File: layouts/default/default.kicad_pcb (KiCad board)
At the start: 2 copper layers, 76.8 x 46.3 mm, 60 parts, among them U10 10µF ±10% 25V X5R, U11 10µF ±10% 25V X5R, U12 10µF ±10% 25V X5R, U13 1MΩ ±1% 62.5mW, U14 100nF ±10% 16V X7R, U16 1µF ±10% 25V X5R, U17 560Ω ±1% 62.5mW, U18 1µF ±10% 25V X5R, U19 4.7kΩ ±1% 62.5mW, U20 10µF ±10% 25V X5R, U21 10µF ±10% 25V X5R, U23 10kΩ ±1% 62.5mW, U25 100nF ±10% 16V X7R, U29 4.7kΩ ±1% 62.5mW, U5 820Ω ±1% 62.5mW, U6 4.7kΩ ±1% 62.5mW, U8 1.5µH ±20%, U9 10µF ±10% 25V X5R

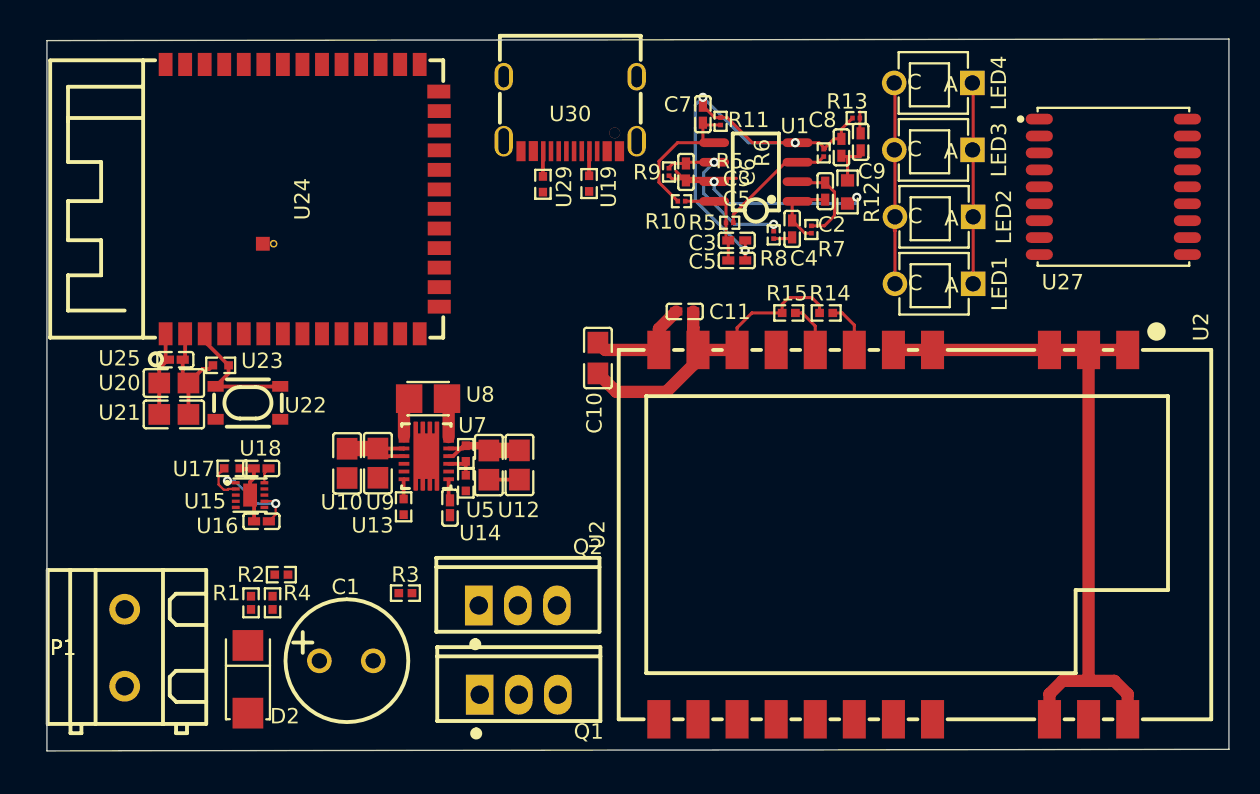
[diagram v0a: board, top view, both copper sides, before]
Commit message: added new oled
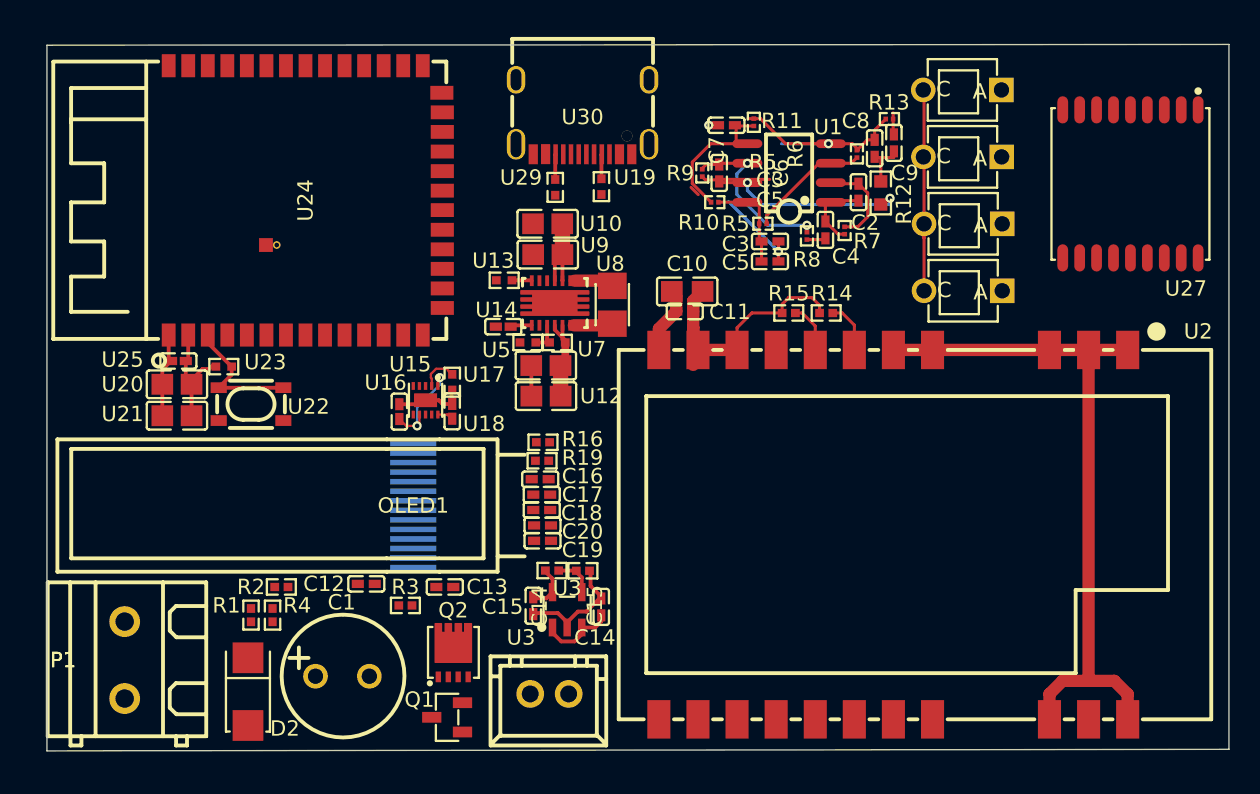
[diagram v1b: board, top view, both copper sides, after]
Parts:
- added C12: 1µF ±10% 25V X5R, atopile:C0402-b3ef17, F.Cu at (54.5, 68.8)
- added C13: 1µF ±10% 25V X5R, atopile:C0402-b3ef17, F.Cu at (59.6, 69.0)
- added C14: 1µF ±10% 25V X5R, atopile:C0402-b3ef17, F.Cu at (69.8, 70.3)
- added C15: 1µF ±10% 25V X5R, atopile:C0402-b3ef17, F.Cu at (65.4, 70.2)
- added C16: 100nF ±10% 16V X7R, atopile:C0402-b3ef17, F.Cu at (65.8, 62.0)
- added C17: 4.7µF ±20% 10V X5R, atopile:C0402-b3ef17, F.Cu at (66.0, 63.0)
- added C18: 100nF ±10% 16V X7R, atopile:C0402-b3ef17, F.Cu at (66.0, 64.0)
- added C19: 100nF ±10% 16V X7R, atopile:C0402-b3ef17, F.Cu at (66.0, 66.0)
- added C20: 100nF ±10% 16V X7R, atopile:C0402-b3ef17, F.Cu at (66.0, 65.0)
- added CN1: , atopile:CONN-TH_XH-2A-b4a6f6, F.Cu at (66.5, 76.0)
- added OLED1: , atopile:OLED-SMD_N087-2832TSWYG02-H14_1-7d3a70, F.Cu at (57.6, 63.7)
- added R16: 510kΩ ±1% 62.5mW, atopile:R0402-56259e, F.Cu at (66.0, 59.6)
- added R17: 10kΩ ±1% 62.5mW, atopile:R0402-56259e, F.Cu at (68.6, 67.9)
- added R18: 25.5kΩ ±1% 62.5mW, atopile:R0402-56259e, F.Cu at (66.6, 67.9)
- added R19: 10kΩ ±1% 62.5mW, atopile:R0402-56259e, F.Cu at (66.0, 60.8)
- added U3: , lib:SOT-23-5_L3.0-W1.7-P0.95-LS2.8-BL, F.Cu at (67.6, 70.5)
- Q1: footprint atopile:TO-220-3_L10.0-W4.5-P2.54-L-8dee21 -> atopile:SOT-23-3_L2.9-W1.3-P1.90-LS2.4-BR-688f29
- Q2: footprint atopile:TO-220-3_L10.0-W4.5-P2.54-L-8dee21 -> atopile:DFN-8_L3.3-W3.3-P0.65-BL-2-bd6bc9
- moved U10 20.3 mm to (66.3, 45.4), turned to 180 degrees
- moved U9 17.5 mm to (66.3, 47.4), turned to 180 degrees
- moved U13 16.1 mm to (63.5, 49.1), turned to 180 degrees
- moved U17 15.4 mm to (60.1, 55.7), turned to -90 degrees
- moved U8 13.4 mm to (70.5, 50.7), turned to 90 degrees
- moved U7 13.0 mm to (66.8, 50.5), turned to 0 degrees
- moved U15 13.0 mm to (58.4, 56.9), turned to 180 degrees
- moved U18 13.0 mm to (60.1, 57.6), turned to 90 degrees
- moved U14 12.3 mm to (63.4, 52.1), turned to 180 degrees
- moved U16 11.4 mm to (56.7, 57.6), turned to 90 degrees
- moved U5 9.99 mm to (65.0, 53.1), turned to 180 degrees
- moved U6 9.36 mm to (67.0, 53.1), turned to 180 degrees
- moved U11 7.45 mm to (66.2, 54.6), turned to 180 degrees
- moved C10 7.24 mm to (75.4, 49.8), turned to 180 degrees
- moved Q2 5.72 mm to (60.2, 74.1)
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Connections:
- net A5 renamed CC1
- net CC2 renamed B5
- net DN2 renamed DN1
- net DP2 renamed DP1
- net VINA renamed boostbuck-EN
- Q1 pad 2: cutoff-C-1 -> gnd
- Q1 pad 3: gnd -> cutoff-C-1
- Q2 pad 1: CUTOFF_GATE -> gnd
- Q2 pad 2: cutoff-C -> gnd
- U15 pad 1: hv-1 -> hv-4
- U15 pad 7: hv-1 -> hv-4
- U16 pad 1: hv-1 -> hv-4
- U20 pad 1: hv-3 -> hv-1
- U21 pad 1: hv-3 -> hv-1
- U23 pad 1: hv-3 -> hv-1
- U24 pad 2: hv-3 -> hv-1
- U24 pad 3: in -> uc-EN
- U25 pad 1: hv-3 -> hv-1
- U27 pad 14: hv-3 -> hv-1
- U27 pad 8: hv-3 -> hv-1
- U30 pad A4: hv-1 -> hv-4
- U30 pad A9: hv-1 -> hv-4
- U30 pad B4: hv-1 -> hv-4
- U30 pad B9: hv-1 -> hv-4
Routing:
- net gnd: track 110.4 -> 90.2 mm
- net hv-4: track 0.00 -> 6.47 mm, vias 0 -> 2
- net hv-3: track 7.52 -> 3.05 mm
- net ADJ_NC: track 0.00 -> 2.56 mm
- net hv-1: track 6.47 -> 7.52 mm, vias 2 -> 0
- net hv-2: track 36.4 -> 35.6 mm
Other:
- board size 76.8 x 46.3 mm -> 76.8 x 45.9 mm

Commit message: added new oled
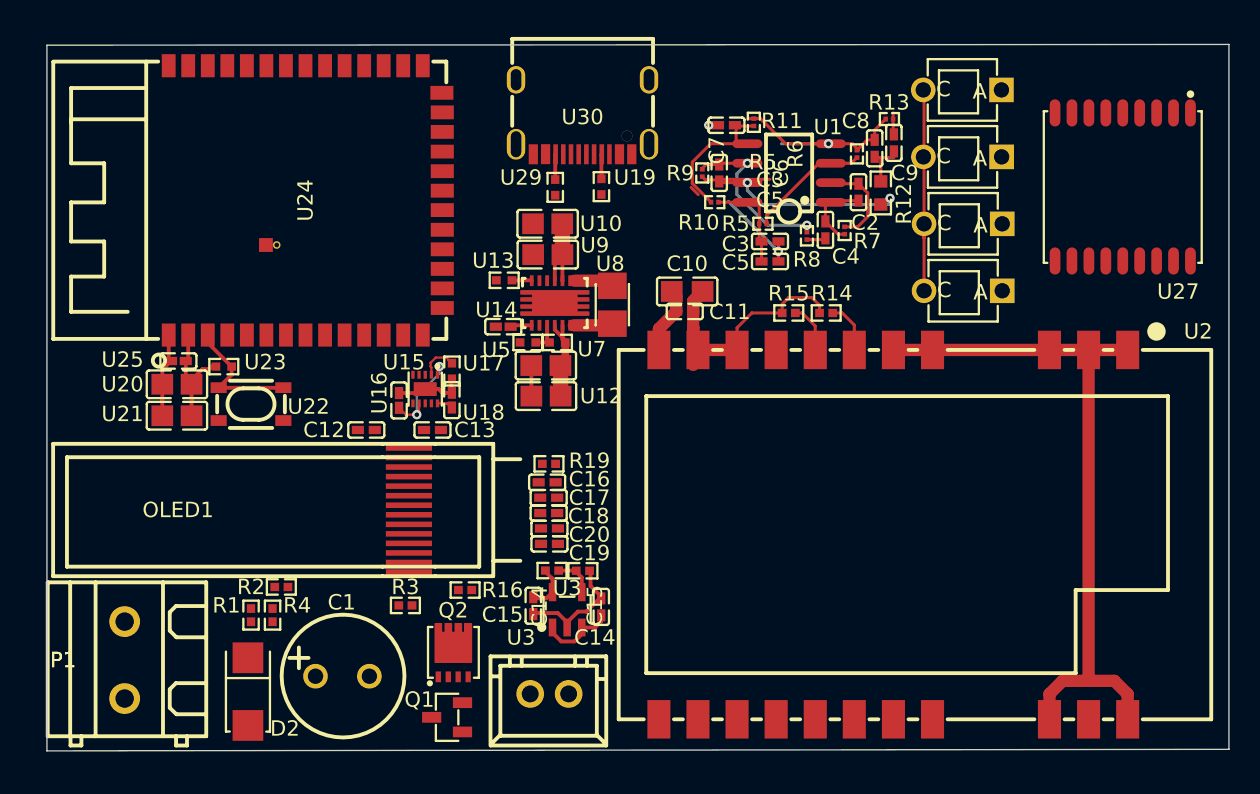
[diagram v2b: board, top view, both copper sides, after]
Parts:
- OLED1: moved to B.Cu
- moved OLED1 15.3 mm to (42.3, 64.0)
- moved R16 10.9 mm to (61.0, 69.2)
- moved C13 10.2 mm to (58.9, 58.8), turned to 180 degrees
- moved C12 10.0 mm to (54.5, 58.8)
- moved U18 0.73 mm to (60.1, 56.9)
- moved U15 0.73 mm to (58.4, 56.1)
- moved U16 0.73 mm to (56.7, 56.9)
- moved U17 0.73 mm to (60.1, 55.0)
- moved U27 0.54 mm to (103.7, 43.0)
- moved C16 0.49 mm to (66.3, 62.2)
- moved C17 0.49 mm to (66.4, 63.2)
- moved C18 0.49 mm to (66.4, 64.2)
- moved C19 0.49 mm to (66.5, 66.2)
- moved C20 0.49 mm to (66.5, 65.2)
- moved R19 0.49 mm to (66.4, 61.0)

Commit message: added new oled
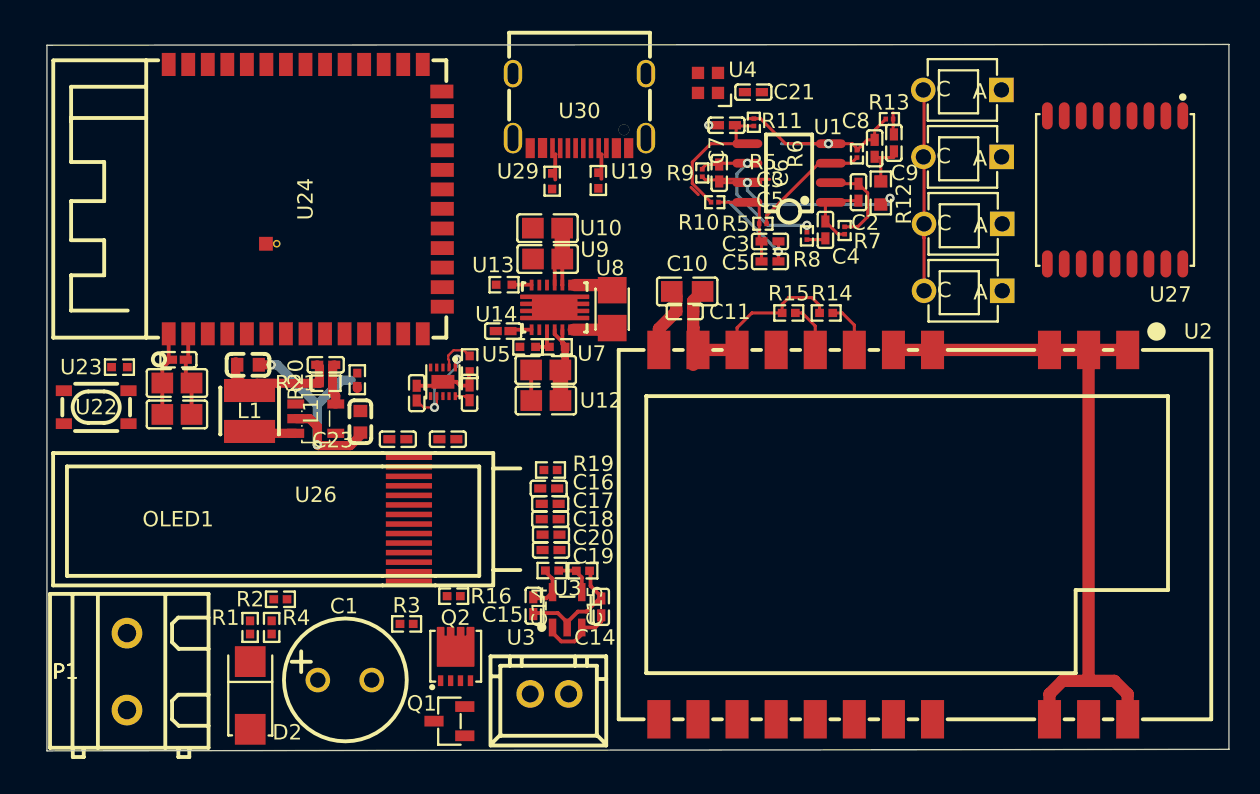
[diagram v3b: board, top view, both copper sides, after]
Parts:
- added C21: 100nF ±10% 16V X7R, atopile:C0402-b3ef17, F.Cu at (79.7, 36.9)
- added C22: 100nF ±10% 16V X7R, atopile:C0402-b3ef17, F.Cu at (51.9, 54.6)
- added C23: 100nF ±10% 50V X7R, atopile:C0603-bd72f6, F.Cu at (54.2, 58.3)
- added C24: 100nF ±10% 50V X7R, atopile:C0603-bd72f6, F.Cu at (46.9, 54.6)
- added L1: , atopile:IND-SMD_L3.0-W3.0-a13401, F.Cu at (47.0, 57.6)
- added R20: 200kΩ ±1% 62.5mW, atopile:R0402-56259e, F.Cu at (54.0, 55.5)
- added R21: 1kΩ ±1% 62.5mW, atopile:R0402-56259e, F.Cu at (51.9, 55.8)
- added U26: , atopile:SOT-23-5_L3.0-W1.7-P0.95-LS2.8-BR-9d80aa, F.Cu at (51.3, 58.1)
- added U4: , lib:LED-SMD_4P-L2.0-W2.0-BR, F.Cu at (76.8, 36.2)
- moved U22 10.1 mm to (37.0, 57.3)
- moved U23 6.78 mm to (38.5, 54.7), turned to 180 degrees
- moved C12 5.33 mm to (59.9, 59.4), turned to 180 degrees
- moved C13 2.33 mm to (56.6, 59.4), turned to 0 degrees
- moved U16 1.24 mm to (57.8, 56.4)
- moved U17 1.24 mm to (61.3, 54.5)
- moved U18 1.24 mm to (61.3, 56.4)
- moved U15 1.24 mm to (59.5, 55.7)
- moved R3 1.20 mm to (57.2, 71.4)
- moved R16 0.84 mm to (60.2, 69.6)
- moved R1 0.80 mm to (47.0, 71.6)
- moved R2 0.80 mm to (49.0, 69.8)
- moved R4 0.80 mm to (48.4, 71.6)
- moved P1 0.76 mm to (39.0, 74.5)
- moved OLED1 0.60 mm to (42.3, 64.6)
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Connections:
- net B5 renamed CC2
- net B8 renamed SUB2
- net CC1 renamed A5
- net DN1 renamed DN2
- net DP1 renamed DP2
- net FB renamed boostbuck-FB
- net SUB1 renamed A8
- net boostbuck-EN renamed VINA
- net detector-net-1 renamed unnamed[1]
- C1 pad 2: cutoff-C-1 -> cutoff-C
- C10 pad 1: hv-2 -> hv
- C11 pad 1: hv-2 -> hv
- C14 pad 1: hv-2 -> hv
- C15 pad 1: hv-3 -> hv-2
- C3 pad 1: hv-2 -> hv
- C5 pad 1: hv-2 -> hv
- CN1 pad 1: hv -> hv-3
- OLED1 pad 5: hv-3 -> hv-2
- P1 pad 2: cutoff-C -> cutoff-C-1
- Q1 pad 3: cutoff-C-1 -> cutoff-C
- Q2 pad 5: cutoff-C -> cutoff-C-1
- R1 pad 1: hv-2 -> hv
- R10 pad 1: hv-2 -> hv
- R14 pad 1: hv-2 -> hv
- R15 pad 1: hv-2 -> hv
- R18 pad 1: hv-3 -> hv-2
- R5 pad 1: hv-2 -> hv
- U1 pad 8: hv-2 -> hv
- U10 pad 1: hv -> hv-3
- U11 pad 1: hv-2 -> hv
- U12 pad 1: hv-2 -> hv
- U15 pad 1: hv-4 -> hv
- U15 pad 10: hv -> hv-3
- U15 pad 7: hv-4 -> hv
- U16 pad 1: hv-4 -> hv
- U18 pad 1: hv -> hv-3
- U2 pad 10: hv-2 -> hv
- U2 pad 9: hv-2 -> hv
- U3 pad 1: hv-2 -> hv
- U3 pad 3: hv-2 -> hv
- U3 pad 5: hv-3 -> hv-2
- U30 pad A4: hv-4 -> hv
- U30 pad A9: hv-4 -> hv
- U30 pad B4: hv-4 -> hv
- U30 pad B9: hv-4 -> hv
- U6 pad 1: hv-2 -> hv
- U7 pad 10: hv -> hv-3
- U7 pad 11: hv -> hv-3
- U7 pad 4: hv-2 -> hv
- U7 pad 5: hv-2 -> hv
- U9 pad 1: hv -> hv-3
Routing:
- net hv: track 6.80 -> 42.0 mm, vias 0 -> 2
- net hv-2: track 35.6 -> 3.05 mm
- net gnd: track 90.2 -> 106.5 mm, vias 3 -> 5
- net in: track 8.62 -> 0.00 mm
- net hv-4: track 6.47 -> 0.00 mm, vias 2 -> 0
- net hv-1: track 7.52 -> 13.7 mm
- net hv-3: track 3.05 -> 6.80 mm
- net SW: track 0.00 -> 3.05 mm
- net ldo-FB: track 0.00 -> 2.81 mm
- net uc-EN: track 0.00 -> 0.50 mm

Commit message: changed layout
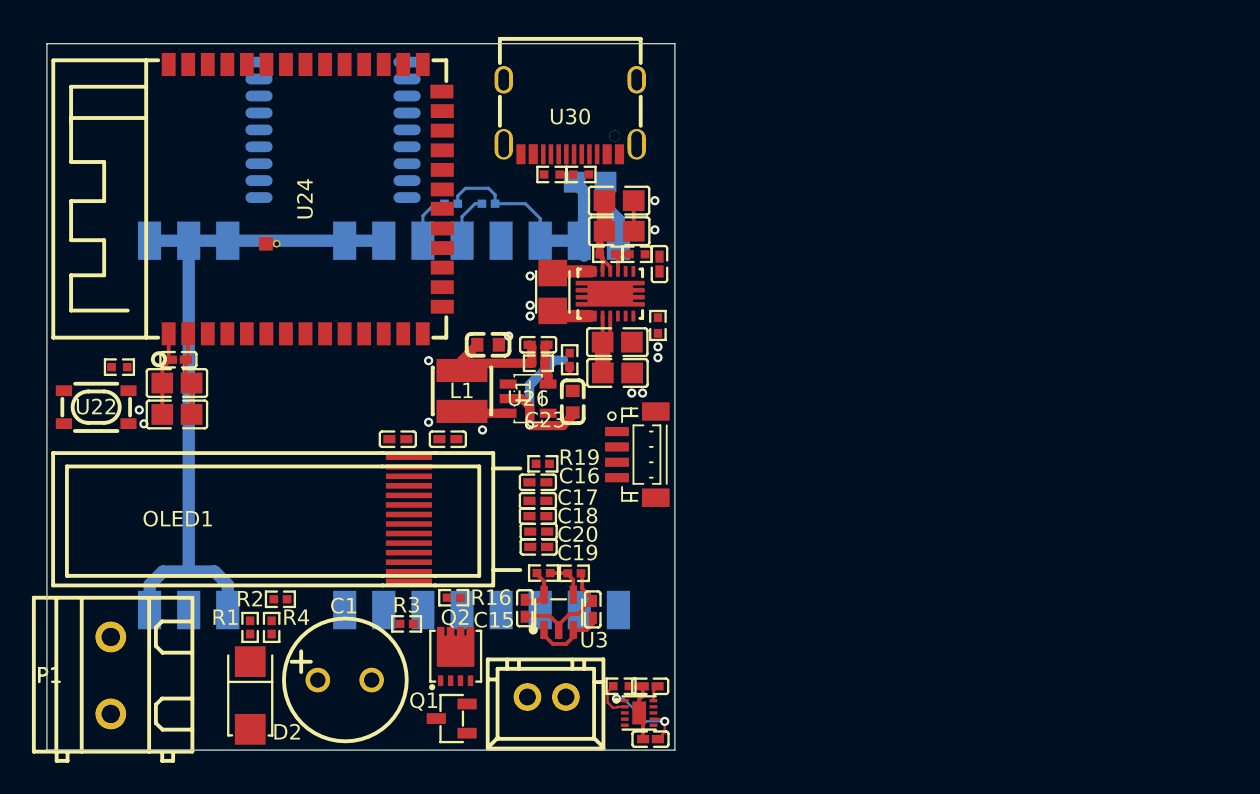
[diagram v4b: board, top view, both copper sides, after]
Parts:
- removed C2, C21, C3, C4, C5, C6, C7, C8, C9: 100nF ±10% 16V X7R, atopile:C0402-b3ef17
- removed LED1, LED2, LED3, LED4: , atopile:SENSOR-TH_BPW34-c0a4b0
- removed R10, R11, R13, R5, R6, R7, R8, R9: 0Ω 50mW, atopile:R0201-27027e
- removed R12: 10kΩ ±1% 100mW, atopile:R0603-ebcab9
- removed U1: , atopile:SOIC-8_L5.0-W4.0-P1.27-LS6.0-BL-294f77
- removed U4: , lib:LED-SMD_4P-L2.0-W2.0-BR
- added CN2: , atopile:CONN-SMD_BM04B-SRSS-TB-6963ef, F.Cu at (72.1, 60.4)
- C10, C11, U2, U27: moved to B.Cu
- R1, R2, R21, R3, R4: value 1kΩ ±1% 62.5mW -> 100kΩ ±1% 62.5mW
- R14, R15: value 1kΩ ±1% 62.5mW -> 100kΩ ±1% 62.5mW; moved to B.Cu
- U5: value 820Ω ±1% 62.5mW -> 100kΩ ±1% 62.5mW
- U6: value 4.7kΩ ±1% 62.5mW -> 560kΩ ±1% 62.5mW
- moved U27 51.0 mm to (52.4, 39.3), turned to -90 degrees
- moved U2 33.8 mm to (55.7, 58.5)
- moved U16 27.1 mm to (73.0, 78.9), turned to 180 degrees
- moved R14 25.4 mm to (60.1, 44.1), turned to 180 degrees
- moved U15 25.0 mm to (72.3, 77.2), turned to -90 degrees
- moved U17 23.1 mm to (71.1, 75.5), turned to 0 degrees
- moved U18 22.4 mm to (73.0, 75.5), turned to 180 degrees
- moved R15 20.8 mm to (62.5, 44.1), turned to 180 degrees
- moved C24 15.7 mm to (62.5, 53.3)
- moved C22 13.9 mm to (65.7, 53.3)
- moved C23 13.9 mm to (68.0, 57.0)
- moved L1 13.9 mm to (60.8, 56.3)
- moved R20 13.9 mm to (67.8, 54.2)
- moved R21 13.9 mm to (65.7, 54.5)
- moved U26 13.9 mm to (65.1, 56.8)
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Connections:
- net A5 renamed CC1
- net A8 renamed SUB1
- net CC2 renamed B5
- net DN2 renamed DN1
- net DP2 renamed DP1
- net VINA renamed boostbuck-EN
- net cutoff-K renamed K
- C10 pad 1: hv -> hv-2
- C11 pad 1: hv -> hv-2
- C14 pad 1: hv -> hv-2
- C15 pad 1: hv-2 -> hv-1
- C16 pad 1: hv-1 -> hv-3
- C17 pad 1: hv-1 -> hv-3
- C18 pad 1: hv-1 -> hv-3
- C19 pad 1: hv-1 -> hv-3
- C20 pad 1: hv-1 -> hv-3
- C22 pad 1: hv-1 -> hv-3
- C24 pad 1: hv-1 -> hv-3
- CN1 pad 1: hv-3 -> hv
- L1 pad 2: hv-1 -> hv-3
- OLED1 pad 13: hv-1 -> hv-3
- OLED1 pad 14: hv-1 -> hv-3
- OLED1 pad 5: hv-2 -> hv-1
- OLED1 pad 8: hv-1 -> hv-3
- R1 pad 1: hv -> hv-2
- R14 pad 1: hv -> hv-2
- R15 pad 1: hv -> hv-2
- R18 pad 1: hv-2 -> hv-1
- R19 pad 2: hv-1 -> hv-3
- R21 pad 1: hv-1 -> hv-3
- U10 pad 1: hv-3 -> hv
- U11 pad 1: hv -> hv-2
- U12 pad 1: hv -> hv-2
- U15 pad 1: hv -> hv-2
- U15 pad 10: hv-3 -> hv
- U15 pad 7: hv -> hv-2
- U16 pad 1: hv -> hv-2
- U18 pad 1: hv-3 -> hv
- U2 pad 10: hv -> hv-2
- U2 pad 9: hv -> hv-2
- U20 pad 1: hv-1 -> hv-3
- U21 pad 1: hv-1 -> hv-3
- U23 pad 1: hv-1 -> hv-3
- U24 pad 2: hv-1 -> hv-3
- U24 pad 38: out -> io2
- U25 pad 1: hv-1 -> hv-3
- U27 pad 14: hv-1 -> hv-3
- U27 pad 8: hv-1 -> hv-3
- U3 pad 1: hv -> hv-2
- U3 pad 3: hv -> hv-2
- U3 pad 5: hv-2 -> hv-1
- U30 pad A4: hv -> hv-2
- U30 pad A9: hv -> hv-2
- U30 pad B4: hv -> hv-2
- U30 pad B9: hv -> hv-2
- U6 pad 1: hv -> hv-2
- U7 pad 10: hv-3 -> hv
- U7 pad 11: hv-3 -> hv
- U7 pad 4: hv -> hv-2
- U7 pad 5: hv -> hv-2
- U9 pad 1: hv-3 -> hv
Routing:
- net hv: track 42.0 -> 6.80 mm, vias 2 -> 0
- net hv-2: track 3.05 -> 35.5 mm, vias 0 -> 2
- net gnd: track 106.5 -> 82.0 mm, vias 5 -> 16
- net detector-K: track 19.1 -> 0.00 mm
- net OUT2: track 17.4 -> 0.00 mm, vias 2 -> 0
- net IN2minus: track 11.3 -> 0.00 mm, vias 2 -> 0
- net hv-1: track 13.7 -> 3.05 mm
- net IN2plus: track 10.4 -> 0.00 mm
- net IN1plus: track 7.96 -> 0.00 mm
- net hv-3: track 6.80 -> 13.5 mm
- net OUT1: track 5.03 -> 0.00 mm
- net unnamed[1]: track 2.82 -> 0.00 mm
- net B5: track 1.65 -> 0.00 mm
- net CC1: track 1.60 -> 0.00 mm
- net out: track 1.42 -> 0.00 mm
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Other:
- board size 76.8 x 45.9 mm -> 40.8 x 45.9 mm
